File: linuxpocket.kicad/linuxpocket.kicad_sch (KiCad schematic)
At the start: 0 parts

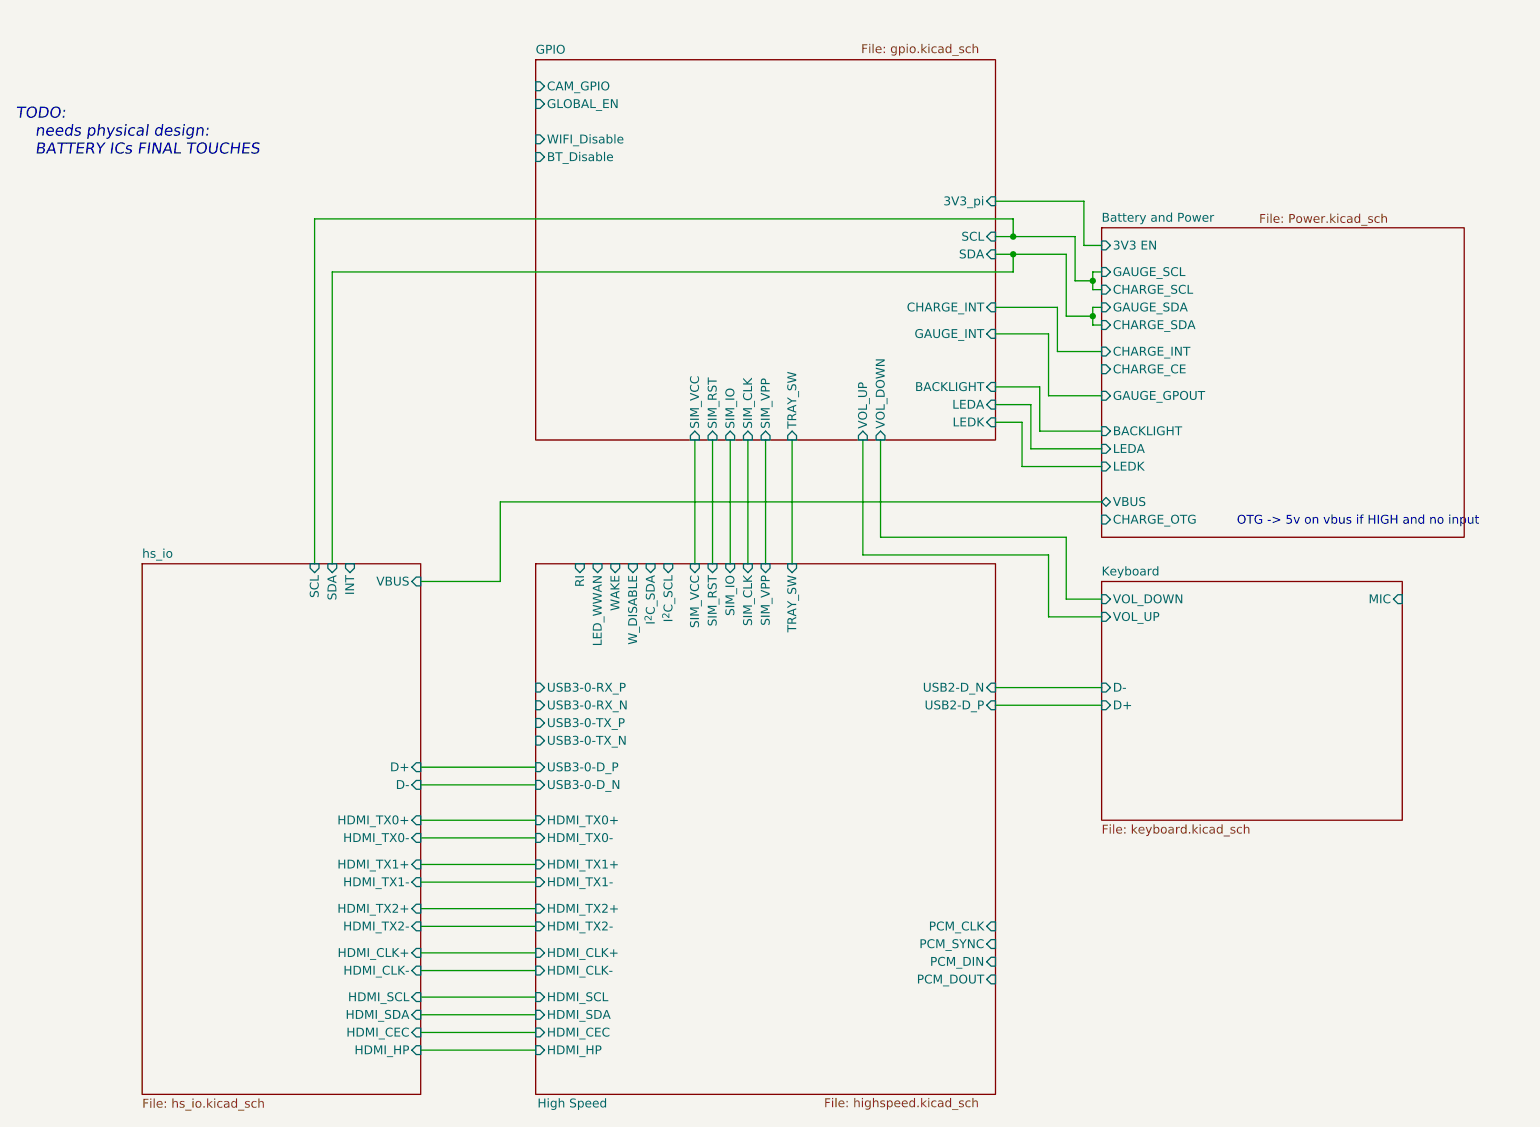
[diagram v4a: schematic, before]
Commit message: Add magnetometer #5. Add footprints to some symbols.
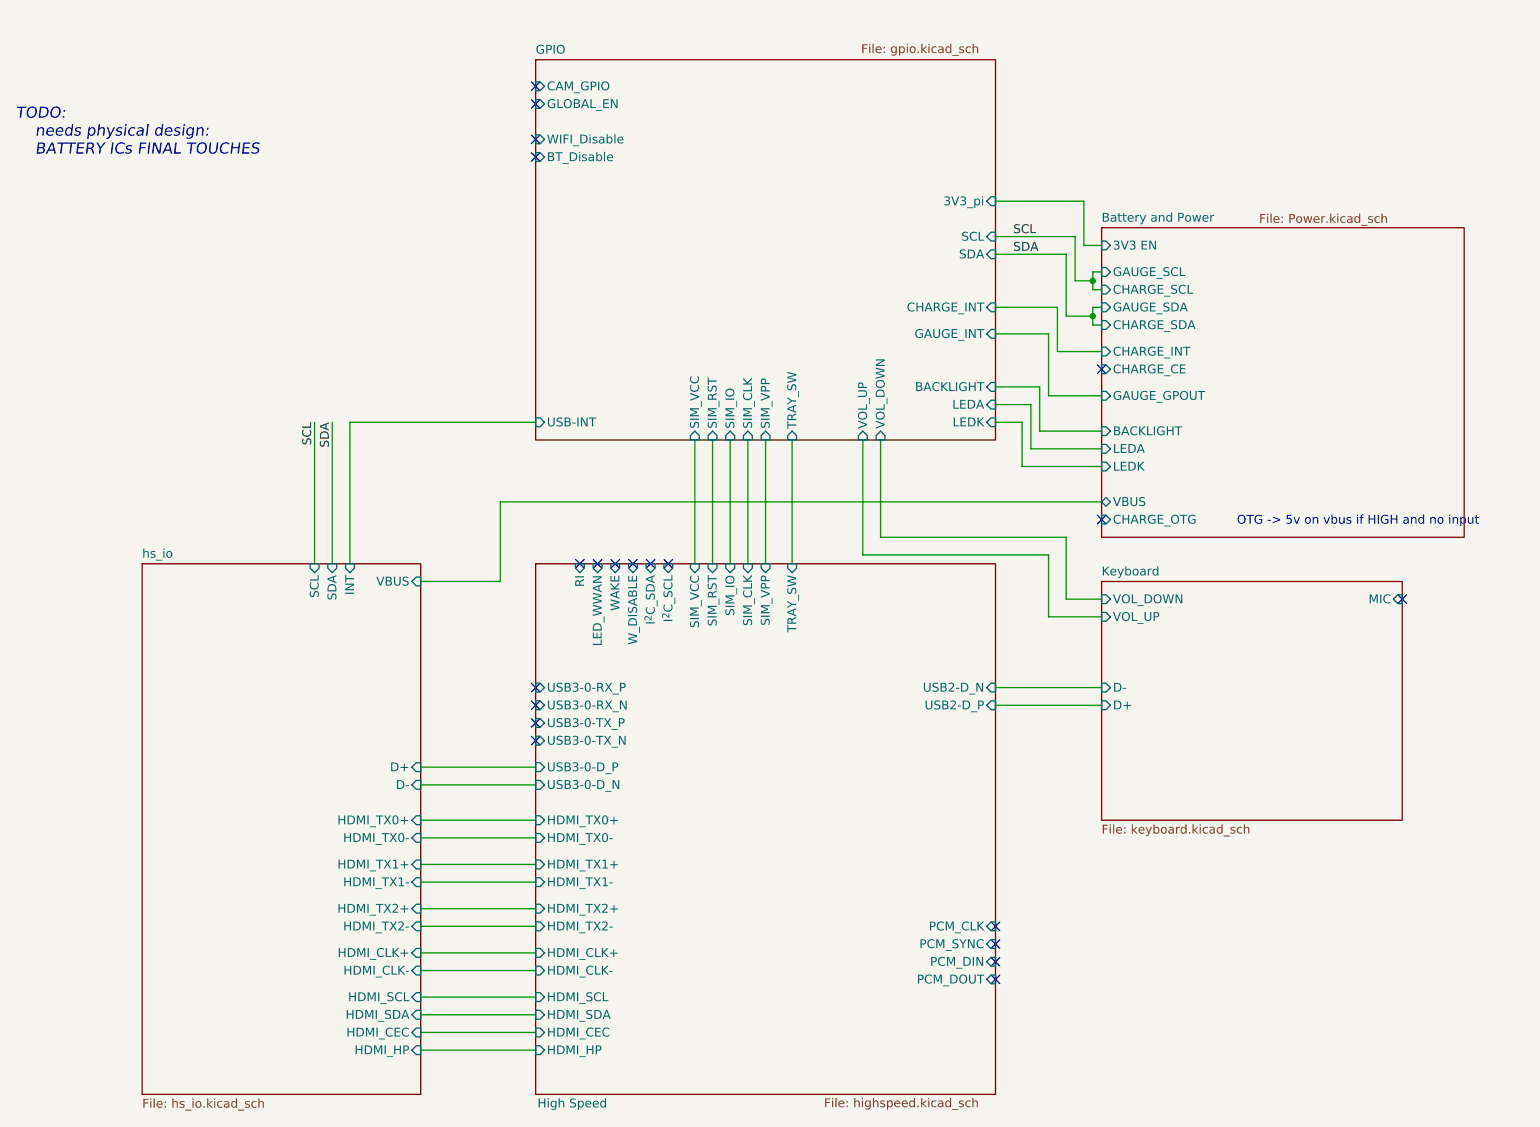
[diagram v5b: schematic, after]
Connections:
- no-connect marks 0 -> 21
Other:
- sheet GPIO ports: added USB-INT; removed none
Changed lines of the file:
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@@
-	)
-	(junction
-		(at 175.26 54.61)
-		(diameter 0)
-		(color 0 0 0 0)
-	)
-	(junction
-		(at 175.26 57.15)
-		(diameter 0)
-		(color 0 0 0 0)
 	)
 	(junction
@@
 		(color 0 0 0 0)
 	)
+	(no_connect
+		(at 115.57 101.6)
+	)
+	(no_connect
+		(at 172.72 156.21)
+	)
+	(no_connect
+		(at 125.73 101.6)
+	)
+	(no_connect
+		(at 187.96 95.25)
+	)
+	(no_connect
+		(at 106.68 127)
+	)
+	(no_connect
+		(at 231.14 106.68)
+	)
+	(no_connect
+		(at 113.03 101.6)
+	)
+	(no_connect
+		(at 106.68 121.92)
+	)
+	(no_connect
+		(at 172.72 161.29)
+	)
+	(no_connect
+		(at 106.68 33.02)
+	)
+	(no_connect
+		(at 123.19 101.6)
+	)
+	(no_connect
+		(at 106.68 124.46)
+	)
+	(no_connect
+		(at 106.68 119.38)
+	)
+	(no_connect
+		(at 187.96 73.66)
+	)
+	(no_connect
+		(at 106.68 40.64)
+	)
+	(no_connect
+		(at 106.68 43.18)
+	)
+	(no_connect
+		(at 106.68 35.56)
+	)
+	(no_connect
+		(at 120.65 101.6)
+	)
+	(no_connect
+		(at 172.72 153.67)
+	)
+	(no_connect
+		(at 118.11 101.6)
+	)
+	(no_connect
+		(at 172.72 158.75)
+	)
 	(wire
 		(pts
@@
 			(width 0)
 			(type default)
+			(color 132 0 0 1)
 		)
 	)
@@
 			(width 0)
 			(type default)
+			(color 132 0 0 1)
 		)
 	)
@@
 	(wire
 		(pts
-			(xy 77.47 101.6) (xy 77.47 59.69)
-		)
-		(stroke
-			(width 0)
-			(type default)
-		)
-	)
-	(wire
-		(pts
 			(xy 139.7 83.82) (xy 139.7 101.6)
 		)
@@
 	(wire
 		(pts
-			(xy 74.93 52.07) (xy 175.26 52.07)
-		)
-		(stroke
-			(width 0)
-			(type default)
-		)
-	)
-	(wire
-		(pts
 			(xy 184.15 54.61) (xy 184.15 60.96)
 		)
@@
 	(wire
 		(pts
-			(xy 175.26 57.15) (xy 182.88 57.15)
+			(xy 172.72 57.15) (xy 182.88 57.15)
 		)
 		(stroke
@@
 	(wire
 		(pts
-			(xy 172.72 57.15) (xy 175.26 57.15)
-		)
-		(stroke
-			(width 0)
-			(type default)
-		)
-	)
-	(wire
-		(pts
 			(xy 186.69 64.77) (xy 187.96 64.77)
 		)
@@
 	(wire
 		(pts
+			(xy 74.93 81.28) (xy 74.93 101.6)
+		)
+		(stroke
+			(width 0)
+			(type default)
+		)
+	)
+	(wire
+		(pts
 			(xy 156.21 97.79) (xy 182.88 97.79)
 		)
@@
 	(wire
 		(pts
-			(xy 175.26 54.61) (xy 184.15 54.61)
-		)
-		(stroke
-			(width 0)
-			(type default)
-		)
-	)
-	(wire
-		(pts
-			(xy 74.93 101.6) (xy 74.93 52.07)
+			(xy 172.72 54.61) (xy 184.15 54.61)
 		)
 		(stroke
@@
 	(wire
 		(pts
+			(xy 77.47 81.28) (xy 77.47 101.6)
+		)
+		(stroke
+			(width 0)
+			(type default)
+		)
+	)
+	(wire
+		(pts
 			(xy 182.88 97.79) (xy 182.88 106.68)
 		)
@@
 	(wire
 		(pts
-			(xy 175.26 59.69) (xy 175.26 57.15)
+			(xy 80.01 81.28) (xy 106.68 81.28)
 		)
 		(stroke
@@
 			(width 0)
 			(type default)
+			(color 132 0 0 1)
 		)
 	)
@@
 	(wire
 		(pts
-			(xy 172.72 54.61) (xy 175.26 54.61)
-		)
-		(stroke
-			(width 0)
-			(type default)
-		)
-	)
-	(wire
-		(pts
 			(xy 186.69 60.96) (xy 186.69 62.23)
 		)
@@
 	(wire
 		(pts
+			(xy 80.01 101.6) (xy 80.01 81.28)
+		)
+		(stroke
+			(width 0)
+			(type default)
+		)
+	)
+	(wire
+		(pts
 			(xy 172.72 49.53) (xy 185.42 49.53)
 		)
@@
 		(pts
 			(xy 132.08 83.82) (xy 132.08 101.6)
-		)
-		(stroke
-			(width 0)
-			(type default)
-		)
-	)
-	(wire
-		(pts
-			(xy 175.26 52.07) (xy 175.26 54.61)
-		)
-		(stroke
-			(width 0)
-			(type default)
-		)
-	)
-	(wire
-		(pts
-			(xy 77.47 59.69) (xy 175.26 59.69)
 		)
 		(stroke
@@
 		)
 	)
+	(label "SDA"
+		(at 175.26 57.15 0)
+		(fields_autoplaced yes)
+		(effects
+			(font
+				(size 1.27 1.27)
+			)
+			(justify left bottom)
+		)
+	)
+	(label "SCL"
+		(at 175.26 54.61 0)
+		(fields_autoplaced yes)
+		(effects
+			(font
+				(size 1.27 1.27)
+			)
+			(justify left bottom)
+		)
+	)
+	(label "SDA"
+		(at 77.47 81.28 270)
+		(fields_autoplaced yes)
+		(effects
+			(font
+				(size 1.27 1.27)
+			)
+			(justify right bottom)
+		)
+	)
+	(label "SCL"
+		(at 74.93 81.28 270)
+		(fields_autoplaced yes)
+		(effects
+			(font
+				(size 1.27 1.27)
+			)
+			(justify right bottom)
+		)
+	)
 	(sheet
 		(at 106.68 29.21)
@@
 			(effects
 				(font
+					(size 1.27 1.27)
+				)
+				(justify left)
+			)
+		)
+		(pin "USB-INT" input
+			(at 106.68 81.28 180)
+			(effects
+				(font

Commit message: PCB almost done and schematic finished.
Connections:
- no-connect marks 21 -> 20
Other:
- sheet GPIO ports: added RI; removed USB-INT
- note removed: "TODO: needs physical design: BATTERY ICs FINAL TOUCHES"
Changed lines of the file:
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@@
-	)
-	(no_connect
-		(at 113.03 101.6)
 	)
 	(no_connect
@@
 		(pts
 			(xy 186.69 59.69) (xy 187.96 59.69)
+		)
+		(stroke
+			(width 0)
+			(type default)
+		)
+	)
+	(wire
+		(pts
+			(xy 113.03 83.82) (xy 113.03 101.6)
 		)
 		(stroke
@@
 		)
 	)
-	(text "TODO:\n	needs physical design:\n	BATTERY ICs FINAL TOUCHES"
-		(exclude_from_sim no)
-		(at 32.004 39.624 0)
-		(effects
-			(font
-				(size 1.6 1.6)
-				(italic yes)
-				(color 194 194 0 1)
-			)
-			(justify left)
-		)
-	)
 	(label "SDA"
 		(at 175.26 57.15 0)
@@
 			)
 		)
-		(pin "USB-INT" input
-			(at 106.68 81.28 180)
-			(effects
-				(font
+		(pin "RI" input
+			(at 113.03 83.82 270)
+			(effects
+				(font
